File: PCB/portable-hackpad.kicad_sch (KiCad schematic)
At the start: 1 part, among them U1 XIAO-RP2040-DIP

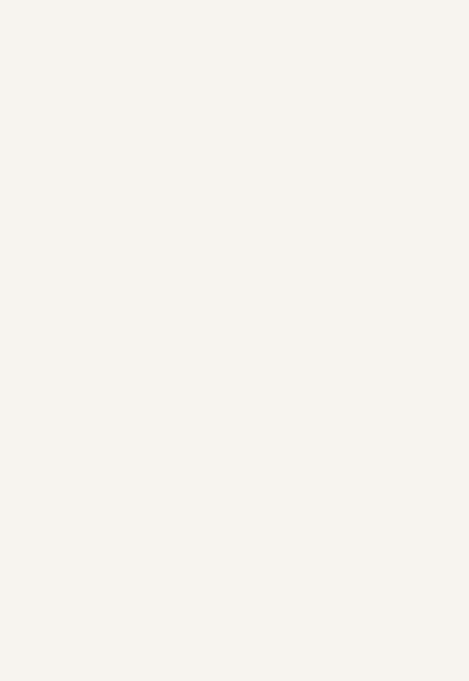
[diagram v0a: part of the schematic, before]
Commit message: added switches to schematic
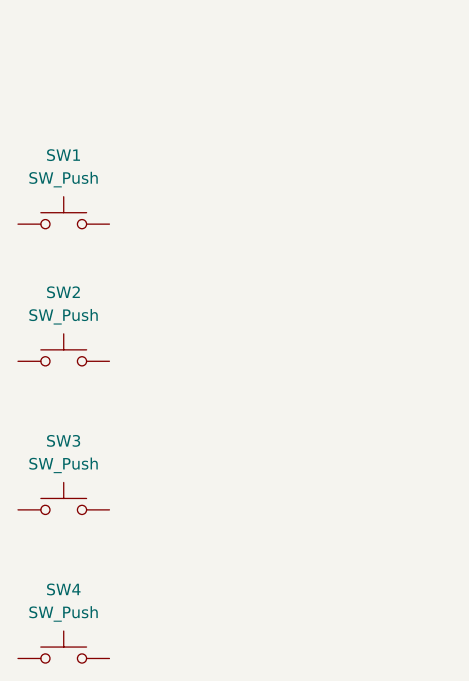
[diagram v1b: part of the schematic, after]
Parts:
- added SW1, SW2, SW3, SW4: SW_Push, symbol Switch:SW_Push

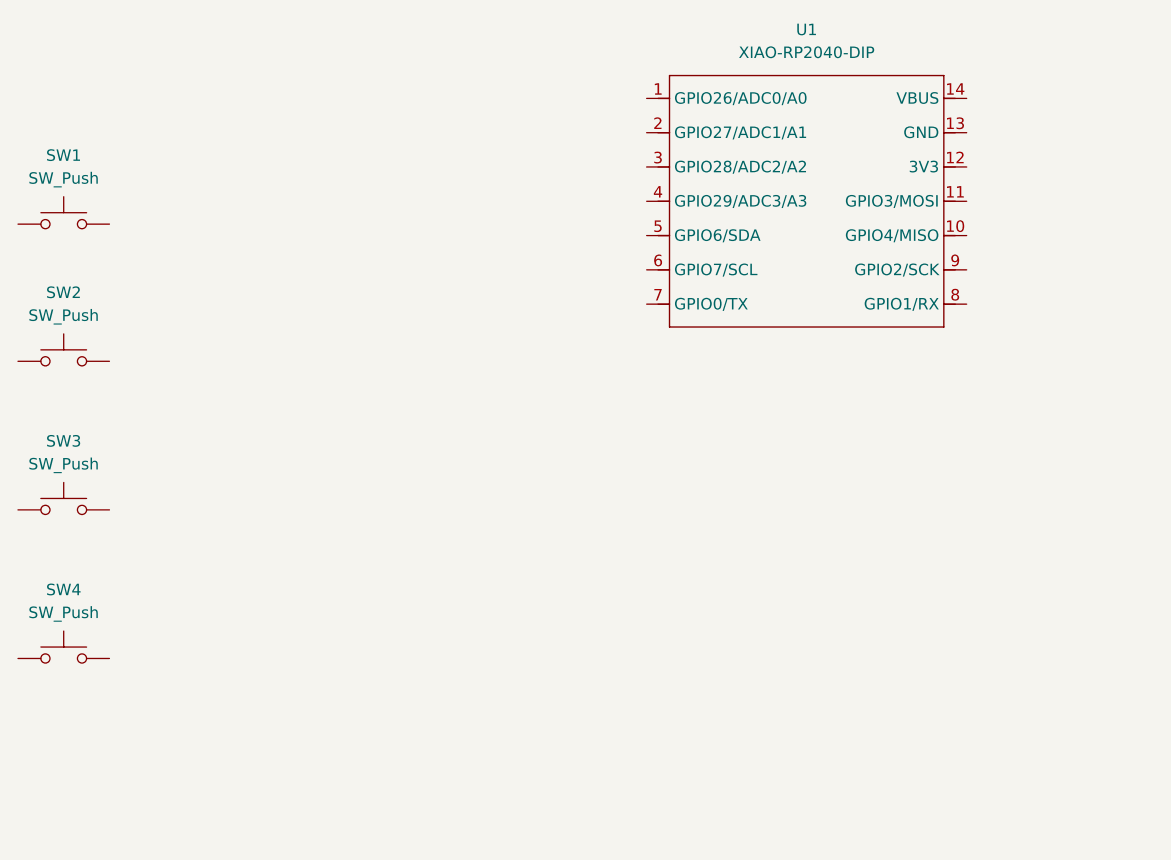
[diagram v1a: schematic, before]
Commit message: neopixels and schematic wiring
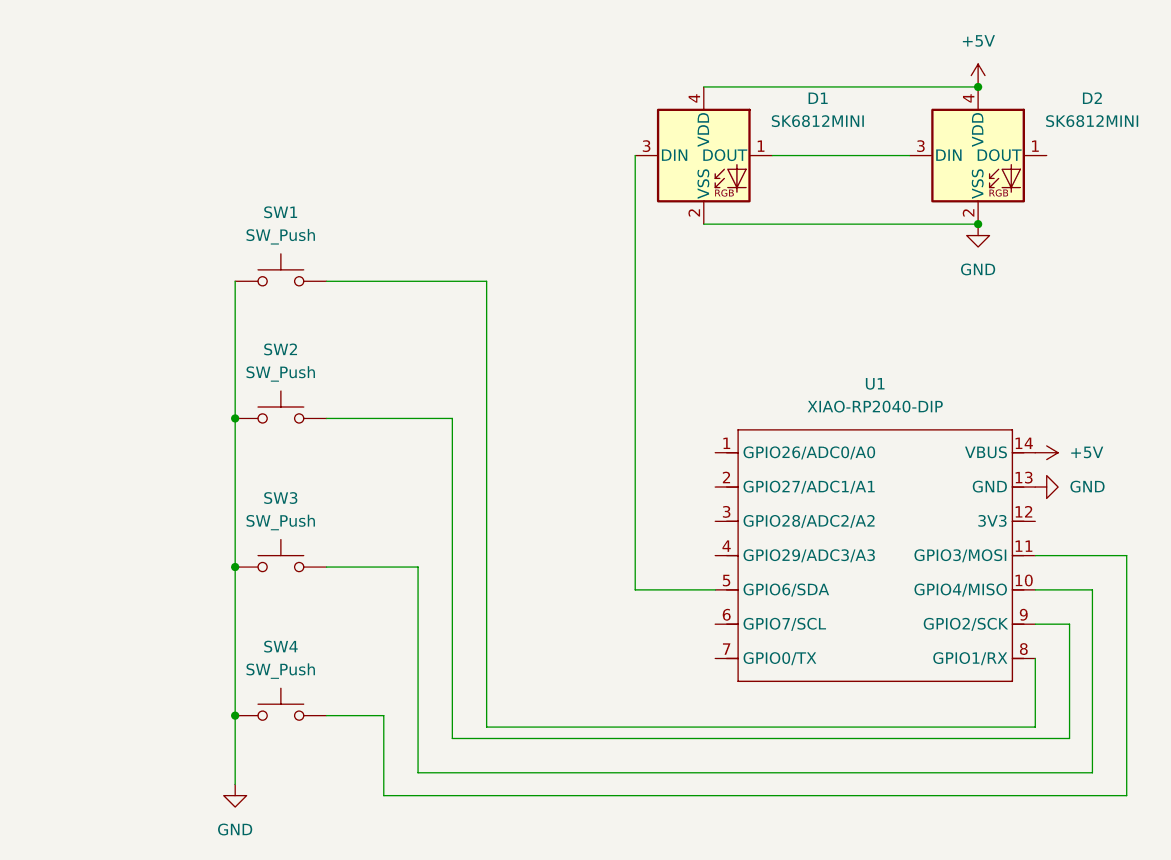
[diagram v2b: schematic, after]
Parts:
- added D1, D2: SK6812MINI, LED_SMD:LED_SK6812MINI_PLCC4_3.5x3.5mm_P1.75mm, symbol LED:SK6812MINI
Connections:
- net GND: now reaches SW2.1
- net GND: now also SW1.1, SW3.1, SW4.1, U1.13 (GND), D1.2 (VSS), D2.2 (VSS)
- net at SW2.2: now also U1.9 (GPIO2/SCK)
- net at SW3.2: now also U1.10 (GPIO4/MISO)
- net at SW4.2: now also U1.11 (GPIO3/MOSI)
- net at SW1.2: now also U1.8 (GPIO1/RX)
- net +5V: now reaches U1.14 (VBUS)
- net +5V: now also D1.4 (VDD), D2.4 (VDD)
- net at U1.5 (GPIO6/SDA): now also D1.3 (DIN)
- new net: D1.1 (DOUT), D2.3 (DIN)
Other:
- moved on the sheet: SW1, SW2, SW3, SW4, U1

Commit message: assigned footprints
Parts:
- SW1, SW2, SW3, SW4: footprint (none) -> Button_Switch_Keyboard:SW_Cherry_MX_1.00u_PCB
- U1: footprint Module:MOUDLE14P-XIAO-DIP-SMD -> OPL:XIAO-RP2040-DIP
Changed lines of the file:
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@@
 			)
 		)
-		(property "Footprint" ""
+		(property "Footprint" "Button_Switch_Keyboard:SW_Cherry_MX_1.00u_PCB"
 			(at 129.54 107.95 0)
 			(effects
@@
 			)
 		)
-		(property "Footprint" ""
+		(property "Footprint" "Button_Switch_Keyboard:SW_Cherry_MX_1.00u_PCB"
 			(at 129.54 124.46 0)
 			(effects
@@
 			)
 		)
-		(property "Footprint" ""
+		(property "Footprint" "Button_Switch_Keyboard:SW_Cherry_MX_1.00u_PCB"
 			(at 129.54 140.97 0)
 			(effects
@@
 			)
 		)
-		(property "Footprint" ""
+		(property "Footprint" "Button_Switch_Keyboard:SW_Cherry_MX_1.00u_PCB"
 			(at 129.54 92.71 0)
 			(effects
@@
 			)
 		)
-		(property "Footprint" "Module:MOUDLE14P-XIAO-DIP-SMD"
+		(property "Footprint" "OPL:XIAO-RP2040-DIP"
 			(at 196.088 144.018 0)
 			(effects
